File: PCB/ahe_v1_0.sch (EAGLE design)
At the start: 19 parts, among them CN1 1X4-BIG, CN3 1X4SMT, IC1 MS560702BA03-50, IC2 MCP73871-1CCI_ML, IC3 TPS7A2055PDBVR, J1 USB3075-30-A

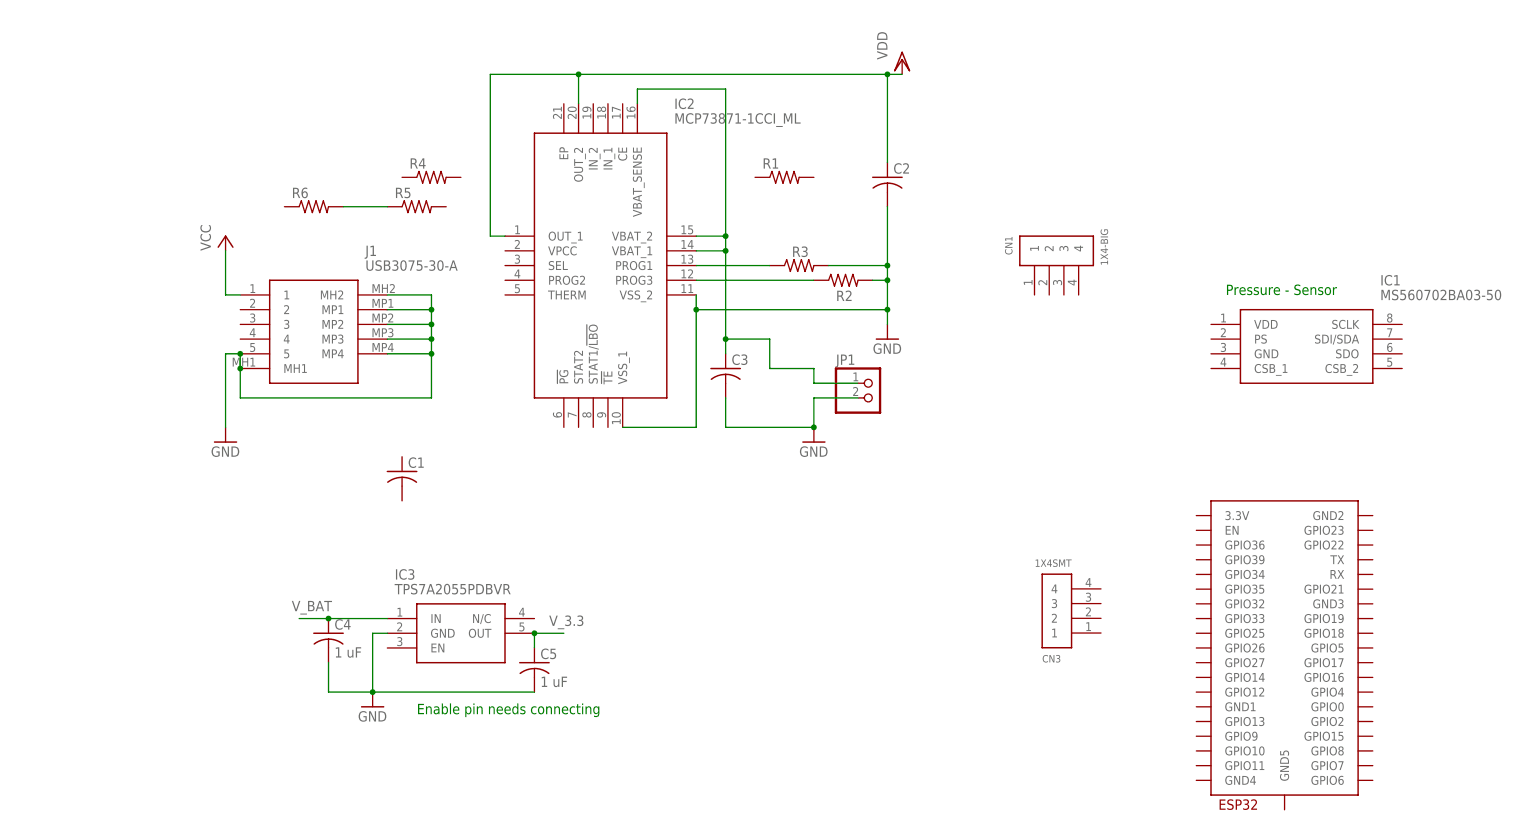
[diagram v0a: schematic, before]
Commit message: Updated the BMS i/o
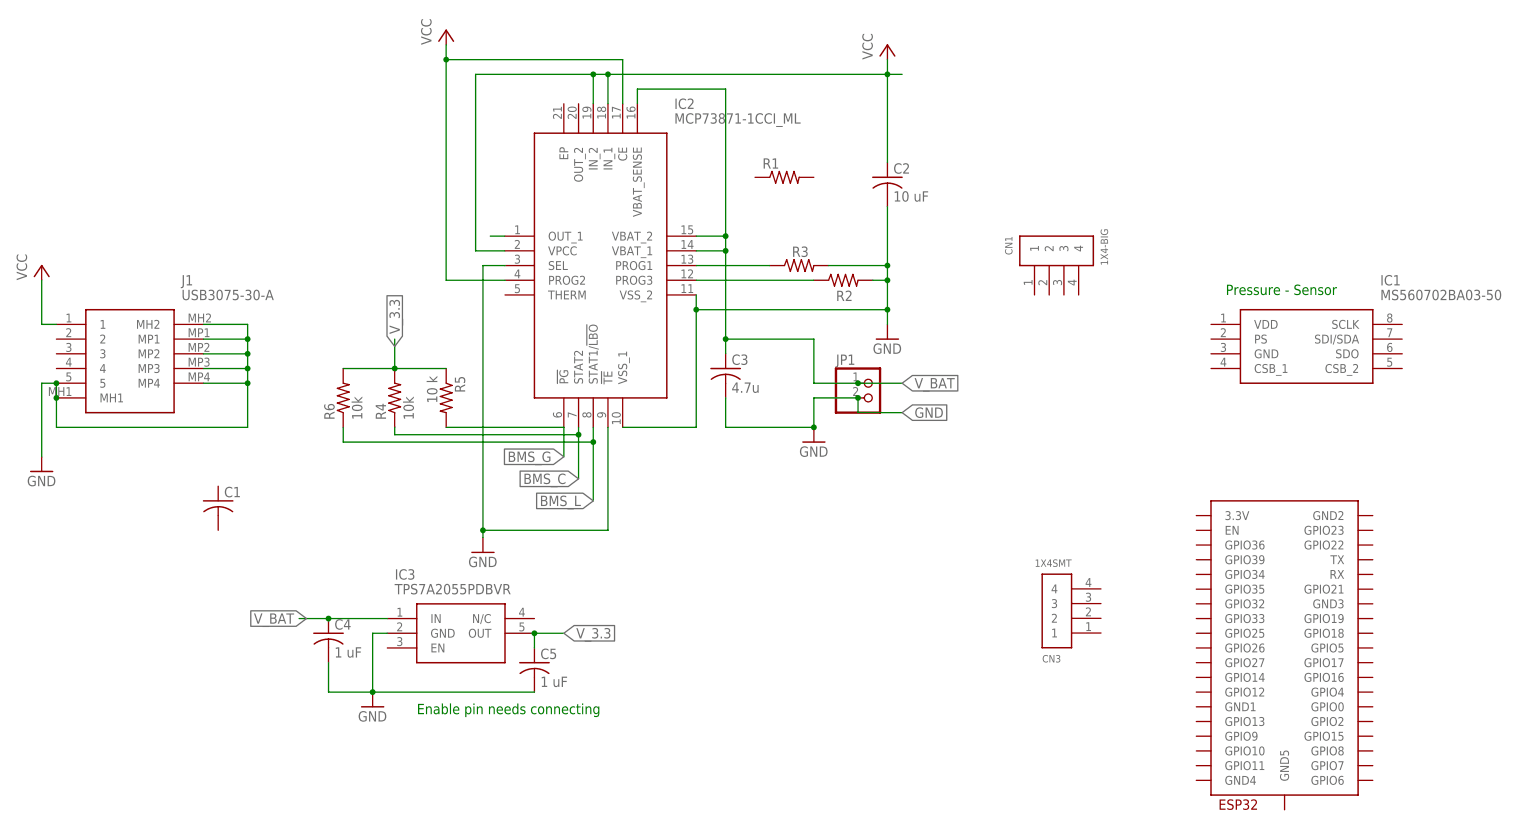
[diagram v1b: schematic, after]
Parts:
- C2: value (none) -> 10 uF
- C3: value (none) -> 4.7u
- R4, R6: value (none) -> 10k
- R5: value (none) -> 10 k
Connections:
- removed net N$3: R5.1, R6.2
- removed net N$4: C3.1, IC2.VBAT_1, IC2.VBAT_2, IC2.VBAT_SENSE, JP1.1
- removed net VDD: C2.1, IC2.OUT_1, IC2.OUT_2
- new net BMS_C: IC2.STAT2, R4.1
- new net BMS_G: IC2.!PG, R5.2
- new net BMS_L: IC2.STAT1/!LBO, R6.1
- new net N$5: IC2.OUT_1
- net GND: now also IC2.!TE, IC2.SEL
- net VCC: now also C2.1, IC2.CE, IC2.IN_1, IC2.IN_2, IC2.PROG2, IC2.VPCC
- net V_3.3: now also R4.2, R5.1, R6.2
- net V_BAT: now also C3.1, IC2.VBAT_1, IC2.VBAT_2, IC2.VBAT_SENSE, JP1.1
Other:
- moved on the sheet: C1, J1, R4, R5, R6
